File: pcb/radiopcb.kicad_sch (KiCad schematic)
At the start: 0 parts

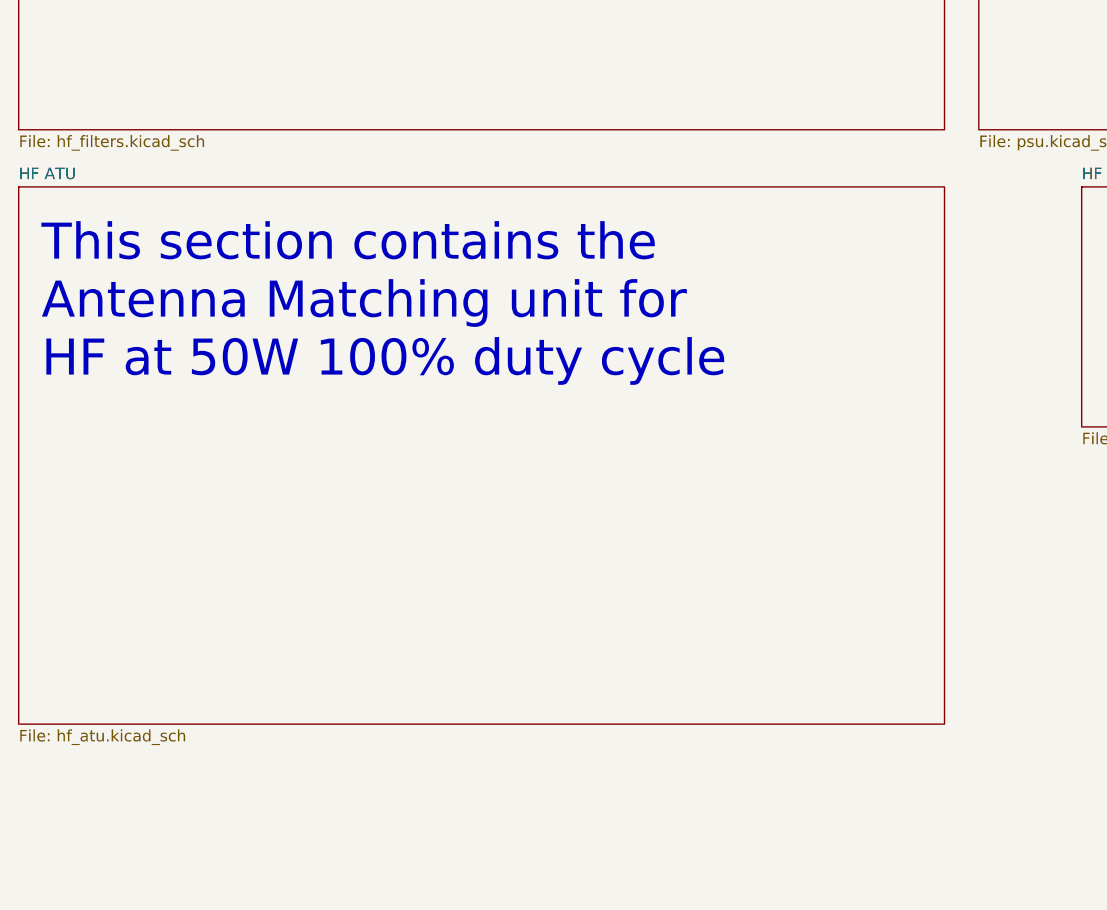
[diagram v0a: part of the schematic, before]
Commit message: cleanup of layout (fixed pcb/ subdirs; stubs for timers
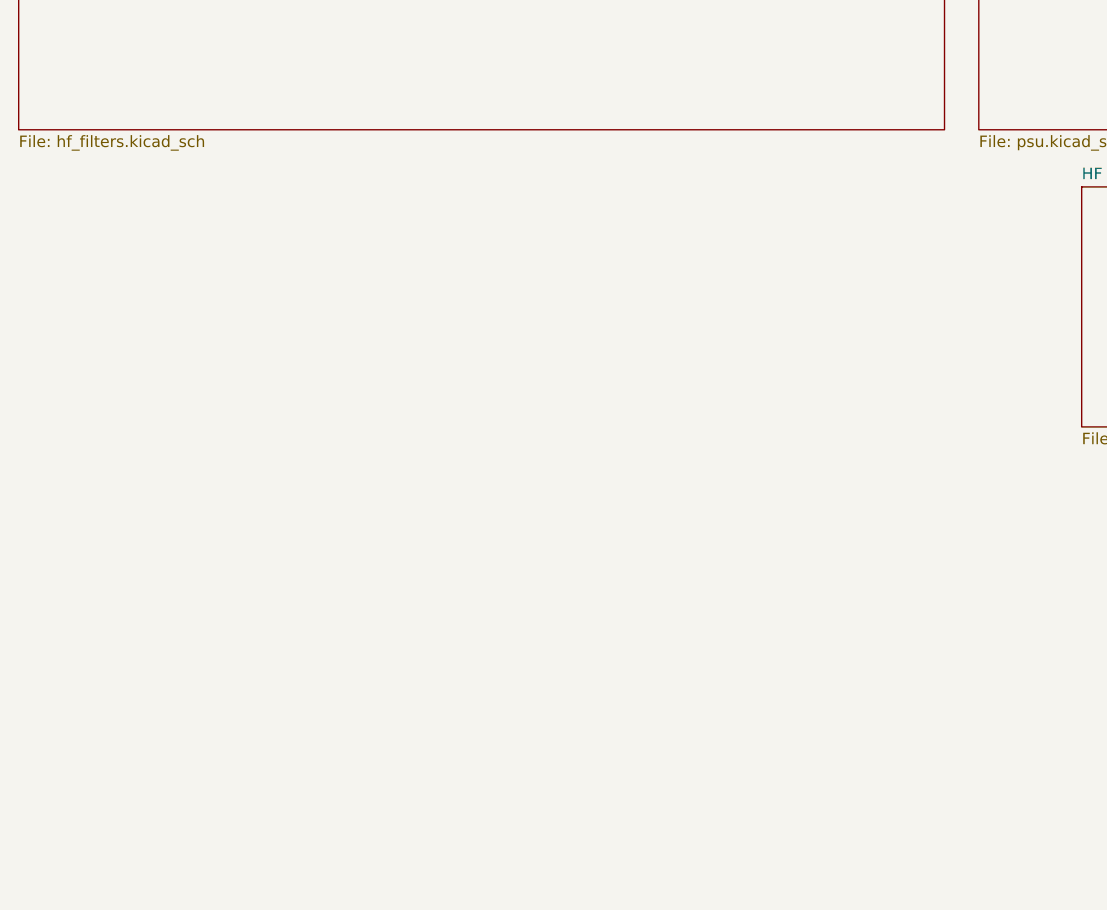
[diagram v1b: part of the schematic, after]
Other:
- removed sheet HF ATU
- note removed: "This section contains the Antenna Matching unit for HF at 50W 100% duty cycle"
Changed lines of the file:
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@@
-		)
-	)
-	(text "This section contains the\nAntenna Matching unit for\nHF at 50W 100% duty cycle"
-		(exclude_from_sim no)
-		(at 16.51 162.56 0)
-		(effects
-			(font
-				(size 4 4)
-			)
-			(justify left bottom)
 		)
 	)
@@
 				)
 			)
-		)
-	)
-	(sheet
-		(at 13.97 140.97)
-		(size 102.87 59.69)
-		(fields_autoplaced yes)
-		(stroke
-			(width 0.1524)
-			(type solid)
-		)
-		(fill
-			(color 0 0 0 0.0000)
-		)
-		(property "Sheetname" "HF ATU"
-			(at 13.97 140.2584 0)
-			(effects
-				(font
-					(size 1.27 1.27)
-				)
-				(justify left bottom)
-			)
-		)
-		(property "Sheetfile" "hf_atu.kicad_sch"
-			(at 13.97 201.2446 0)
-			(effects
-				(font
-					(size 1.27 1.27)
-				)
-				(justify left top)
-			)
-		)
-		(instances
-			(project "radiopcb"
-				(path "/7de6637b-a3f9-4235-bc7f-a0209db4fd87"
-					(page "3")
-				)
-			)
